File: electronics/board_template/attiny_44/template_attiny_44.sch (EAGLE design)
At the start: 16 parts, among them IC2 ATTINY44A-MU, IC3 NCP1117ST50T3G, J1 GROVE_CONNECTOR2.0_1X4, J2 GROVE_CONNECTOR2.0_1X4, J3 10129383-906001ALF, Y1 X322516MLB4SI

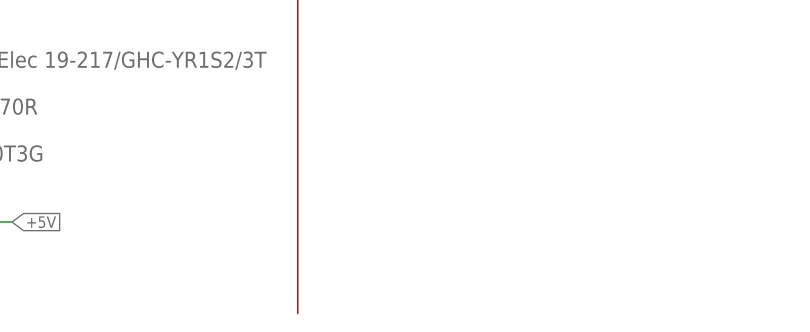
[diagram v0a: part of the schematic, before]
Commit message: Logo hinzugefügt
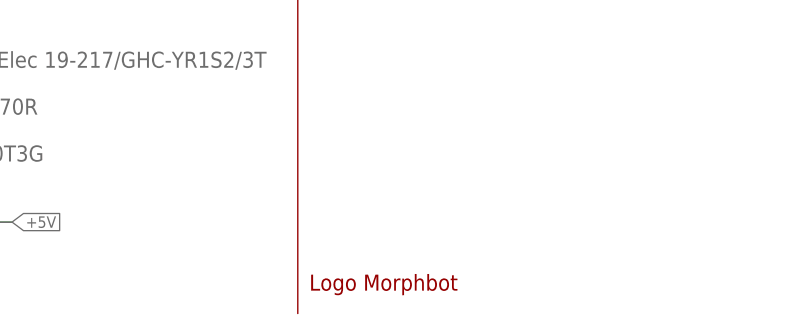
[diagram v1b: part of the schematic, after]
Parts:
- added U$1: LOGO_MORPHBOT5MM, topo-eng:LOGO_MORPHBOT5MM
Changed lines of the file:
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@@
 <layer number="104" name="Name" color="7" fill="1" visible="no" active="yes"/>
 <layer number="116" name="Patch_BOT" color="9" fill="4" visible="no" active="yes"/>
+<layer number="120" name="brd_placement_notes" color="7" fill="1" visible="yes" active="yes"/>
 <layer number="121" name="_tsilk" color="7" fill="1" visible="no" active="yes"/>
 <layer number="122" name="_bsilk" color="7" fill="1" visible="no" active="yes"/>
+<layer number="144" name="DrillLegend" color="7" fill="1" visible="yes" active="yes"/>
+<layer number="145" name="DrillLegend_01-16" color="7" fill="1" visible="yes" active="yes"/>
+<layer number="146" name="DrillLegend_01-20" color="7" fill="1" visible="yes" active="yes"/>
 <layer number="151" name="HeatSink" color="14" fill="1" visible="no" active="no"/>
+<layer number="198" name="BMP198" color="7" fill="1" visible="yes" active="yes"/>
+<layer number="199" name="Contour" color="7" fill="1" visible="yes" active="yes"/>
 <layer number="200" name="200bmp" color="1" fill="10" visible="no" active="no"/>
 <layer number="201" name="201bmp" color="2" fill="1" visible="no" active="no"/>
@@
 <layer number="207" name="207bmp" color="15" fill="10" visible="no" active="no"/>
 <layer number="208" name="208bmp" color="9" fill="10" visible="no" active="yes"/>
+<layer number="209" name="Route9Document" color="7" fill="1" visible="yes" active="yes"/>
+<layer number="210" name="Route10Document" color="7" fill="1" visible="yes" active="yes"/>
+<layer number="211" name="Route11Document" color="7" fill="1" visible="yes" active="yes"/>
+<layer number="212" name="Route12Document" color="7" fill="1" visible="yes" active="yes"/>
+<layer number="213" name="Route13Document" color="7" fill="1" visible="yes" active="yes"/>
+<layer number="214" name="Route14Document" color="7" fill="1" visible="yes" active="yes"/>
+<layer number="215" name="Route15Document" color="7" fill="1" visible="yes" active="yes"/>
+<layer number="216" name="BottomDocument" color="7" fill="1" visible="yes" active="yes"/>
+<layer number="220" name="DimensionDocument" color="7" fill="1" visible="yes" active="yes"/>
+<layer number="221" name="tPlaceDocument" color="7" fill="1" visible="yes" active="yes"/>
+<layer number="222" name="bPlaceDocument" color="7" fill="1" visible="yes" active="yes"/>
+<layer number="225" name="tNamesDocument" color="7" fill="1" visible="yes" active="yes"/>
+<layer number="226" name="bNamesDocument" color="7" fill="1" visible="yes" active="yes"/>
+<layer number="227" name="tValuesDocument" color="7" fill="1" visible="yes" active="yes"/>
+<layer number="228" name="bValuesDocument" color="7" fill="1" visible="yes" active="yes"/>
+<layer number="229" name="tStopDocument" color="7" fill="1" visible="yes" active="yes"/>
+<layer number="230" name="bStopDocument" color="7" fill="1" visible="yes" active="yes"/>
+<layer number="231" name="tCreamDocument" color="7" fill="1" visible="yes" active="yes"/>
+<layer number="232" name="bCreamDocument" color="7" fill="1" visible="yes" active="yes"/>
+<layer number="233" name="tFinishDocument" color="7" fill="1" visible="yes" active="yes"/>
+<layer number="234" name="bFinishDocument" color="7" fill="1" visible="yes" active="yes"/>
+<layer number="235" name="tGlueDocument" color="7" fill="1" visible="yes" active="yes"/>
+<layer number="236" name="bGlueDocument" color="7" fill="1" visible="yes" active="yes"/>
+<layer number="244" name="DrillsDocument" color="7" fill="1" visible="yes" active="yes"/>
+<layer number="245" name="HolesDocument" color="7" fill="1" visible="yes" active="yes"/>
+<layer number="246" name="MillingDocument" color="7" fill="1" visible="yes" active="yes"/>
+<layer number="247" name="MeasuresDocument" color="7" fill="1" visible="yes" active="yes"/>
 <layer number="250" name="Descript" color="3" fill="1" visible="no" active="no"/>
 <layer number="251" name="SMDround" color="12" fill="11" visible="no" active="no"/>
@@
 <part name="IC3" library="samacsys" deviceset="NCP1117ST50T3G" device=""/>
 <part name="C7" library="rcl" library_urn="urn:adsk.eagle:library:334" deviceset="CPOL-EU" device="C" package3d_urn="urn:adsk.eagle:package:23422/2" value="ST(Semtech) CK1C470M-CRD54 - 47uF"/>
+<part name="U$1" library="topo-eng" library_urn="urn:adsk.eagle:library:6646478" deviceset="LOGO_MORPHBOT" device="5MM"/>
 </parts>
 <sheets>
@@
 <attribute name="VALUE" x="21.463" y="38.5826" size="1.778" layer="96"/>
 </instance>
+<instance part="U$1" gate="G$1" x="88.9" y="2.54" smashed="yes"/>
 </instances>
 <busses>
